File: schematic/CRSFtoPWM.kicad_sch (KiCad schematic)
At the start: 30 parts, among them J1 Bat+, J2 UART1/Rx, J3 ICSP, J4 TSW-104-08-G-T-RA, J5 TSW-104-08-G-T-RA, J6 TSW-104-08-G-T-RA, J7 TSW-102-08-L-T-RA, U1 AP7375-50W5-7, U2 AP2210N-3.3TRG1, U3 ATSAMD21E18A-MU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

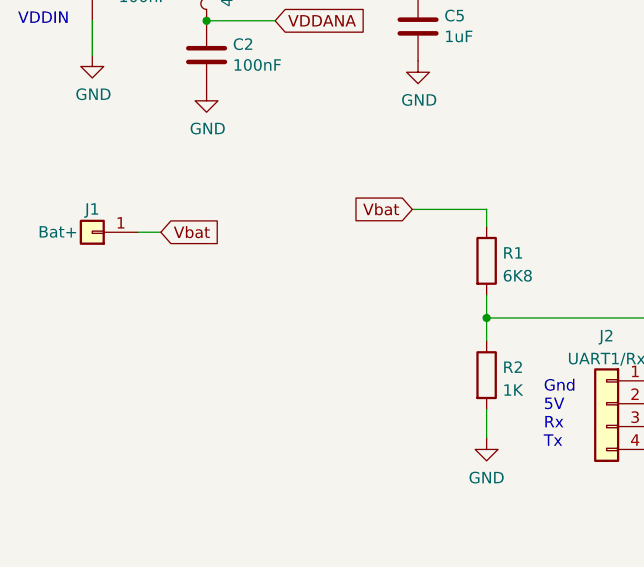
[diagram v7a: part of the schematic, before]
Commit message: Added jumper to allow power from VServo
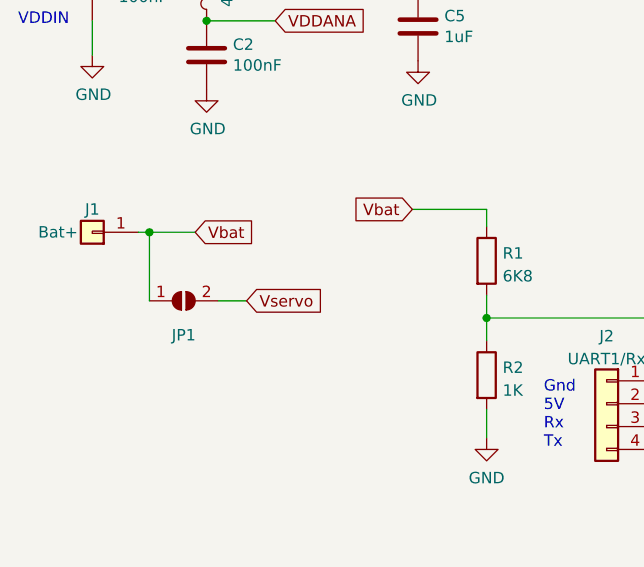
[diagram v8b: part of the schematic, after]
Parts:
- added JP1: SolderJumper_2_Open, Jumper:SolderJumper-2_P1.3mm_Open_RoundedPad1.0x1.5mm, symbol Jumper:SolderJumper_2_Open
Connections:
- net Vbat: now also JP1.1 (A)
- net Vservo: now also JP1.2 (B)
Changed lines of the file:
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@@
   (junction (at 158.115 66.04) (diameter 0) (color 0 0 0 0)
+  )
+  (junction (at 36.195 66.675) (diameter 0) (color 0 0 0 0)
   )
   (junction (at 138.43 24.765) (diameter 0) (color 0 0 0 0)
@@
     (stroke (width 0) (type default) (color 0 0 0 0))
   )
+  (wire (pts (xy 43.815 74.295) (xy 46.99 74.295))
+    (stroke (width 0) (type default) (color 0 0 0 0))
+  )
   (wire (pts (xy 37.465 134.62) (xy 43.18 134.62))
     (stroke (width 0) (type default) (color 0 0 0 0))
@@
     (stroke (width 0) (type default) (color 0 0 0 0))
   )
+  (wire (pts (xy 36.195 66.675) (xy 41.275 66.675))
+    (stroke (width 0) (type default) (color 0 0 0 0))
+  )
   (wire (pts (xy 160.02 70.485) (xy 160.02 80.645))
     (stroke (width 0) (type default) (color 0 0 0 0))
@@
     (stroke (width 0) (type default) (color 0 0 0 0))
   )
+  (wire (pts (xy 36.195 66.675) (xy 36.195 74.295))
+    (stroke (width 0) (type default) (color 0 0 0 0))
+  )
   (wire (pts (xy 123.19 32.385) (xy 123.19 55.245))
     (stroke (width 0) (type default) (color 0 0 0 0))
@@
     (stroke (width 0) (type default) (color 0 0 0 0))
   )
-  (wire (pts (xy 34.925 66.675) (xy 37.465 66.675))
+  (wire (pts (xy 34.925 66.675) (xy 36.195 66.675))
     (stroke (width 0) (type default) (color 0 0 0 0))
   )
@@
     )
   )
-  (global_label "Vbat" (shape input) (at 37.465 66.675 0) (fields_autoplaced)
+  (global_label "Vbat" (shape input) (at 41.275 66.675 0) (fields_autoplaced)
     (effects (font (size 1.27 1.27)) (justify left))
-    (property "Intersheet References" "${INTERSHEET_REFS}" (id 0) (at 43.9905 66.7544 0)
+    (property "Intersheet References" "${INTERSHEET_REFS}" (id 0) (at 47.8005 66.7544 0)
+      (effects (font (size 1.27 1.27)) (justify left) hide)
+    )
+  )
+  (global_label "Vservo" (shape input) (at 46.99 74.295 0) (fields_autoplaced)
+    (effects (font (size 1.27 1.27)) (justify left))
+    (property "Intersheet References" "${INTERSHEET_REFS}" (id 0) (at 55.5112 74.2156 0)
       (effects (font (size 1.27 1.27)) (justify left) hide)
     )
@@
     )
     (pin "1")
+  )
+  (symbol (lib_id "Jumper:SolderJumper_2_Open") (at 40.005 74.295 0) (unit 1)
+    (in_bom yes) (on_board yes)
+    (property "Reference" "JP1" (id 0) (at 40.005 78.105 0))
+    (property "Value" "SolderJumper_2_Open" (id 1) (at 40.005 72.2431 0)
+      (effects (font (size 1.27 1.27)) hide)
+    )
+    (property "Footprint" "Jumper:SolderJumper-2_P1.3mm_Open_RoundedPad1.0x1.5mm" (id 2) (at 40.005 74.295 0)
+      (effects (font (size 1.27 1.27)) hide)
+    )
+    (property "Datasheet" "~" (id 3) (at 40.005 74.295 0)
+      (effects (font (size 1.27 1.27)) hide)
+    )
+    (pin "1")
+    (pin "2")
   )
   (symbol (lib_id "power:+3V3") (at 245.745 142.875 270) (unit 1)
@@
       (reference "J7") (unit 1) (value "TSW-102-08-L-T-RA") (footprint "SamacSys_Parts:HDRRA6W64P254_3X2_508X254X810P")
     )
+    (path "/1c0dd955-674b-4d6a-9215-339a75fed94f"
+      (reference "JP1") (unit 1) (value "SolderJumper_2_Open") (footprint "Jumper:SolderJumper-2_P1.3mm_Open_RoundedPad1.0x1.5mm")
+    )
     (path "/3afb7e41-12a2-422e-a825-777bcbc81b04"
